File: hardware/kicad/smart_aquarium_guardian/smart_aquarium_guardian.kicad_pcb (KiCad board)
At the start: 2 copper layers, 106.7 x 90.2 mm, 29 parts, among them J1 Display_2.8_TFT_240xRGBx320, J2 Tiny_RTC_I2C_Module, J3 SensorsInput, J4 TdsMeter, J5 PowerSupply, M1 MountingHole_3.5mm, M2 MountingHole_3.5mm, M3 MountingHole_3.5mm, M4 MountingHole_3.5mm

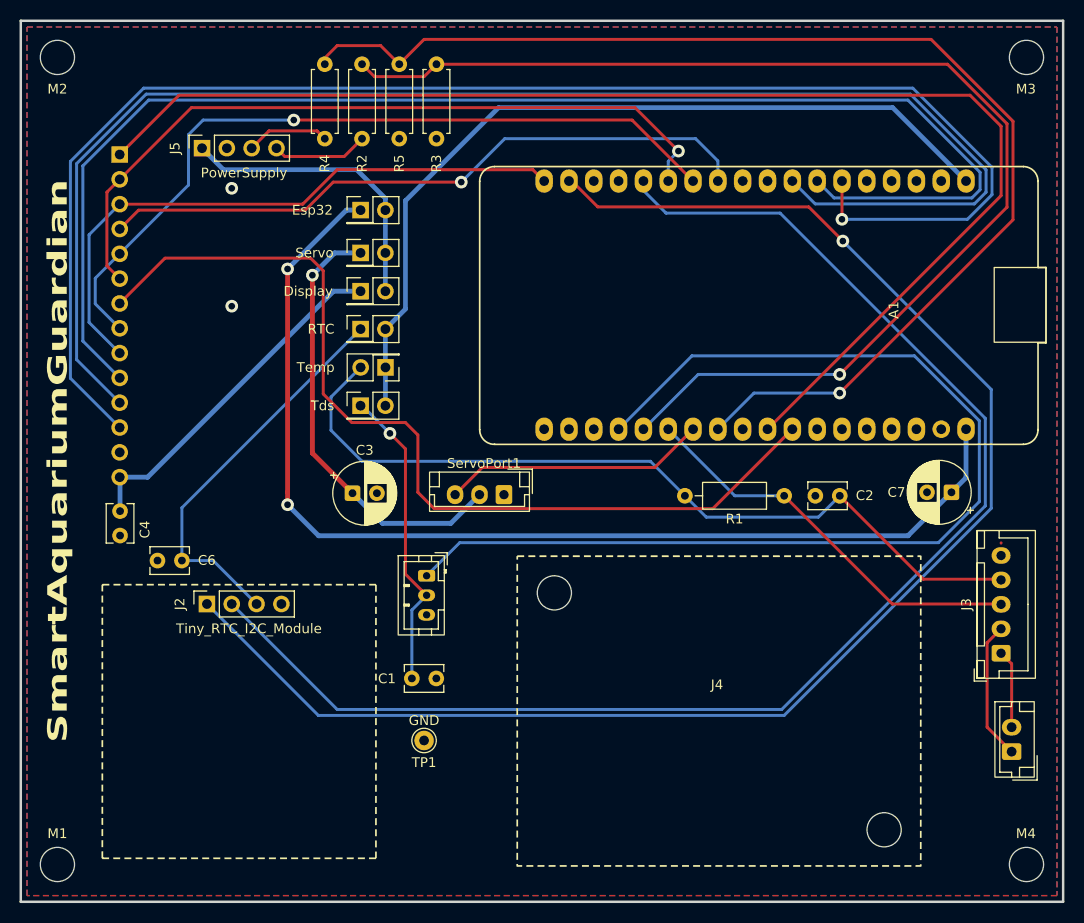
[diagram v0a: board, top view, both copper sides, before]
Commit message: First draft completed for the power supply kicad project
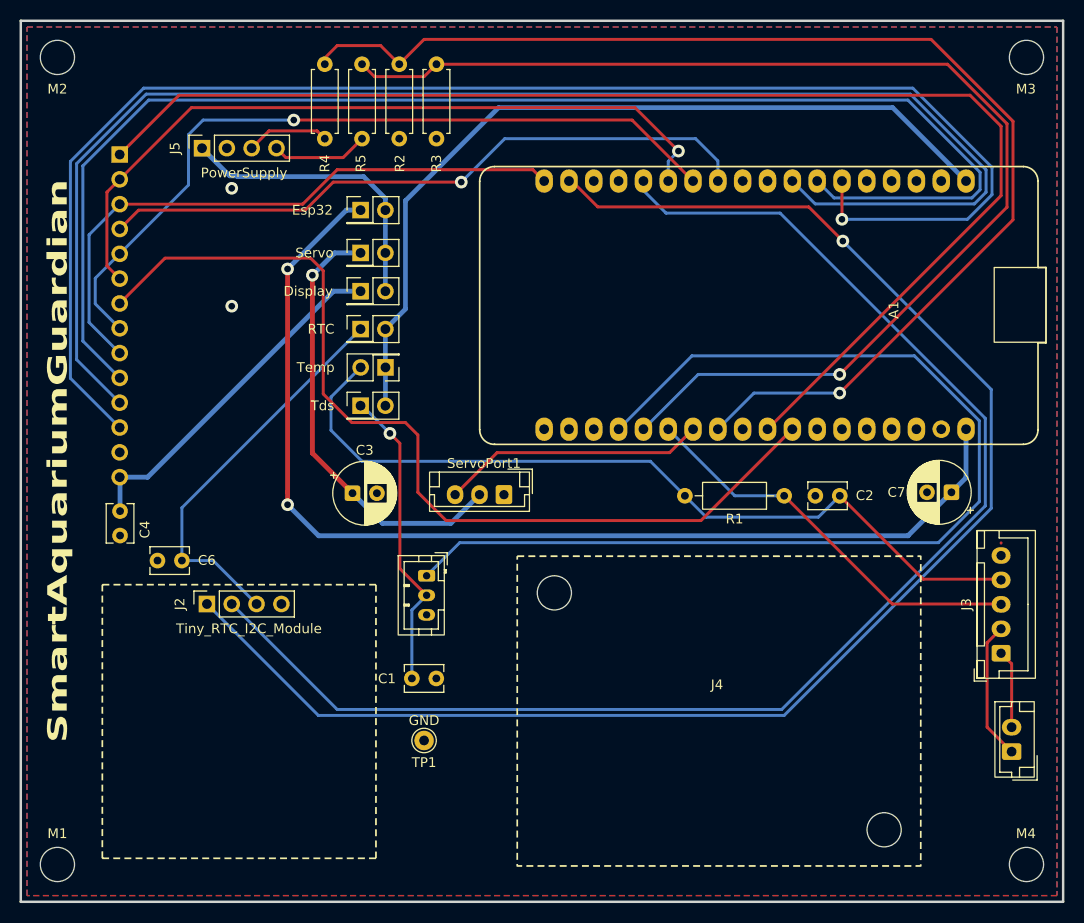
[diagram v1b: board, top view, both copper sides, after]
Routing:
- net Net-(A1-ADC2_CH6/D14): track 95.6 -> 96.6 mm
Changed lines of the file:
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@@
 		(tags "Resistor Axial_DIN0207 series Axial Horizontal pin pitch 7.62mm 0.25W = 1/4W length 6.3mm diameter 2.5mm")
 		(property "Reference" "R2"
-			(at -2.54 -3.81 90)
+			(at -2.535 0.065 90)
 			(layer "F.SilkS")
 			(effects
@@
 		(tags "Resistor Axial_DIN0207 series Axial Horizontal pin pitch 7.62mm 0.25W = 1/4W length 6.3mm diameter 2.5mm")
 		(property "Reference" "R5"
-			(at 10.16 -3.81 90)
+			(at 10.155 0.125 90)
 			(layer "F.SilkS")
 			(effects
@@
 	)
 	(segment
-		(start 113.11093 72.7191)
-		(end 128.018079 72.7191)
+		(start 167.965 99.575)
+		(end 141.88 99.575)
 		(width 0.3048)
 		(layer "F.Cu")
@@
 	)
 	(segment
-		(start 129.3009 74.001921)
-		(end 129.3009 86.6133)
+		(start 138.99 90.8166)
+		(end 137.72 89.5466)
 		(width 0.3048)
 		(layer "F.Cu")
@@
 	)
 	(segment
-		(start 177.315 90.225)
-		(end 169.1828 98.3572)
+		(start 132.2342 89.5466)
+		(end 129.3009 86.6133)
 		(width 0.3048)
 		(layer "F.Cu")
@@
 	)
 	(segment
-		(start 132.2342 89.5466)
-		(end 137.72 89.5466)
+		(start 113.11093 72.7191)
+		(end 108.475 77.35503)
 		(width 0.3048)
 		(layer "F.Cu")
@@
 	)
 	(segment
-		(start 169.1828 98.3572)
-		(end 140.6622 98.3572)
+		(start 177.315 90.225)
+		(end 167.965 99.575)
 		(width 0.3048)
 		(layer "F.Cu")
@@
 	)
 	(segment
-		(start 138.99 90.8166)
-		(end 137.72 89.5466)
+		(start 128.018079 72.7191)
+		(end 113.11093 72.7191)
 		(width 0.3048)
 		(layer "F.Cu")
@@
 	)
 	(segment
-		(start 140.6622 98.3572)
-		(end 138.99 96.685)
+		(start 138.99 96.685)
+		(end 138.99 90.8166)
 		(width 0.3048)
 		(layer "F.Cu")
@@
 	)
 	(segment
-		(start 108.475 77.35503)
-		(end 113.11093 72.7191)
+		(start 129.3009 86.6133)
+		(end 129.3009 74.001921)
 		(width 0.3048)
 		(layer "F.Cu")
@@
 	)
 	(segment
-		(start 129.3009 86.6133)
-		(end 132.2342 89.5466)
+		(start 129.3009 74.001921)
+		(end 128.018079 72.7191)
 		(width 0.3048)
 		(layer "F.Cu")
@@
 	)
 	(segment
-		(start 138.99 96.685)
-		(end 138.99 90.8166)
+		(start 141.88 99.575)
+		(end 138.99 96.685)
 		(width 0.3048)
 		(layer "F.Cu")
@@
 	)
 	(segment
-		(start 128.018079 72.7191)
-		(end 129.3009 74.001921)
+		(start 137.72 89.5466)
+		(end 132.2342 89.5466)
 		(width 0.3048)
 		(layer "F.Cu")
@@
 	)
 	(segment
-		(start 142.8 96.924)
-		(end 145.579 94.145)
+		(start 164.755 92.625)
+		(end 167.155 90.225)
 		(width 0.3048)
 		(layer "F.Cu")
@@
 	)
 	(segment
-		(start 163.235 94.145)
-		(end 167.155 90.225)
+		(start 147.099 92.625)
+		(end 164.755 92.625)
 		(width 0.3048)
 		(layer "F.Cu")
@@
 	)
 	(segment
-		(start 145.579 94.145)
-		(end 163.235 94.145)
+		(start 142.8 96.924)
+		(end 147.099 92.625)
 		(width 0.3048)
 		(layer "F.Cu")
@@
 	)
 	(segment
+		(start 120.542466 64.375)
+		(end 120.466466 64.299)
+		(width 0.4826)
+		(layer "B.Cu")
+		(net 33)
+	)
+	(segment
 		(start 135.665 72.183)
 		(end 135.665 76.104)
@@
 	)
 	(segment
-		(start 119.1 63.665)
-		(end 116.9 61.465)
+		(start 133.438081 64.375)
+		(end 120.542466 64.375)
 		(width 0.4826)
 		(layer "B.Cu")
@@
 	)
 	(segment
+		(start 120.466466 64.299)
+		(end 119.734 64.299)
+		(width 0.4826)
+		(layer "B.Cu")
+		(net 33)
+	)
+	(segment
 		(start 135.665 67.804)
 		(end 135.665 66.601919)
@@
 	(segment
 		(start 135.665 66.601919)
-		(end 132.728081 63.665)
+		(end 133.438081 64.375)
 		(width 0.4826)
 		(layer "B.Cu")
@@
 	)
 	(segment
-		(start 132.728081 63.665)
-		(end 119.1 63.665)
+		(start 119.734 64.299)
+		(end 116.9 61.465)
 		(width 0.4826)
 		(layer "B.Cu")
@@
 	)
 	(segment
-		(start 125.37 62.315)
-		(end 131.45 62.315)
+		(start 124.52 61.465)
+		(end 125.48 62.425)
 		(width 0.3048)
 		(layer "F.Cu")
@@
 	)
 	(segment
-		(start 131.45 62.315)
+		(start 131.34 62.425)
 		(end 133.275 60.49)
 		(width 0.3048)
@@
 	)
 	(segment
-		(start 124.52 61.465)
-		(end 125.37 62.315)
+		(start 125.48 62.425)
+		(end 131.34 62.425)
 		(width 0.3048)
 		(layer "F.Cu")
@@
 	)
 	(segment
-		(start 137.72 105.06)
-		(end 139.885 107.225)
+		(start 137.15 91.67)
+		(end 137.15 104.49)
 		(width 0.3048)
 		(layer "F.Cu")
@@
 	)
 	(segment
-		(start 136.1325 90.6525)
-		(end 137.72 92.24)
+		(start 137.15 104.49)
+		(end 139.885 107.225)
 		(width 0.3048)
 		(layer "F.Cu")
@@
 	)
 	(segment
-		(start 137.72 92.24)
-		(end 137.72 105.06)
+		(start 136.1325 90.6525)
+		(end 137.15 91.67)
 		(width 0.3048)
 		(layer "F.Cu")

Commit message: Visual changes on KiCAD projects
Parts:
- C3: value 100u -> 470u
- C7: value 220u -> 1000u
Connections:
- net Net-(A1-ADC1_CH4/D32) renamed /TEMP_DATA
- net Net-(A1-ADC1_CH5/D33) renamed /SERVO_PWM
- net Net-(A1-ADC1_CH6/D34) renamed /TDS_DATA
- net Net-(A1-ADC1_CH7/D35) renamed /V_BAT*
- net Net-(A1-ADC2_CH6/D14) renamed /LED_BKL
- net Net-(A1-ADC2_CH7/D27) renamed /LED_IRQ_{touch}
- net Net-(A1-D15) renamed /LED_CS
- net Net-(A1-D18) renamed /LED_SCK
- net Net-(A1-D19) renamed /LED_SDO
- net Net-(A1-D2) renamed /LED_DO
- net Net-(A1-D21/SDA) renamed /RTC_SDA
- net Net-(A1-D22/SCL) renamed /RTC_SCL
- net Net-(A1-D23) renamed /LED_SDI
- net Net-(A1-D4) renamed /LED_RST
- net Net-(A1-D5) renamed /LED_CS_{touch}
- net Net-(A1-DAC1/ADC2_CH8/D25) renamed /V_USB*
